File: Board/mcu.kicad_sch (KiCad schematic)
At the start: 16 parts, among them J2 Conn_01x03_Pin, U2 RP2040

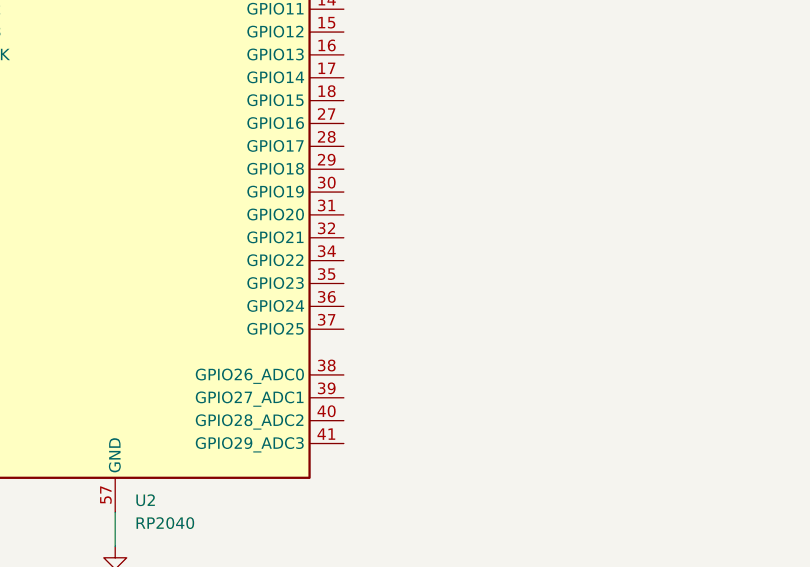
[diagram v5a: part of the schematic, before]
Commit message: Done routing all parts.
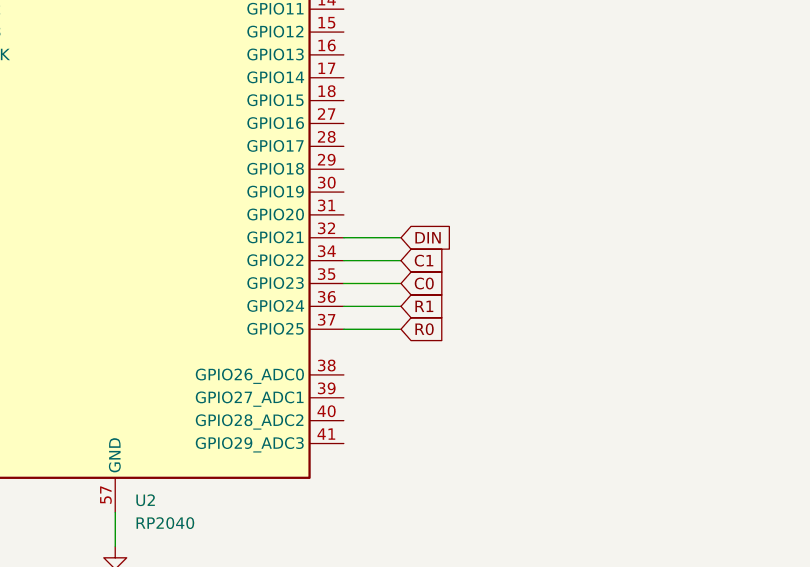
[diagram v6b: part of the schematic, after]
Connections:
- net DIN: now reaches U2.32 (GPIO21)
- net C1: now reaches U2.34 (GPIO22)
- net C0: now reaches U2.35 (GPIO23)
- net R1: now reaches U2.36 (GPIO24)
- net R0: now reaches U2.37 (GPIO25)
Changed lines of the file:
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@@
+    (stroke (width 0) (type default))
+  )
+  (wire (pts (xy 135.89 135.89) (xy 142.24 135.89))
     (stroke (width 0) (type default))
   )
@@
     (stroke (width 0) (type default))
   )
+  (wire (pts (xy 135.89 140.97) (xy 142.24 140.97))
+    (stroke (width 0) (type default))
+  )
   (wire (pts (xy 118.11 63.5) (xy 118.11 72.39))
     (stroke (width 0) (type default))
@@
     (stroke (width 0) (type default))
   )
+  (wire (pts (xy 135.89 133.35) (xy 142.24 133.35))
+    (stroke (width 0) (type default))
+  )
   (wire (pts (xy 105.41 63.5) (xy 107.95 63.5))
     (stroke (width 0) (type default))
@@
     (stroke (width 0) (type default))
   )
+  (wire (pts (xy 135.89 138.43) (xy 142.24 138.43))
+    (stroke (width 0) (type default))
+  )
   (wire (pts (xy 125.73 49.53) (xy 138.43 49.53))
     (stroke (width 0) (type default))
@@
   )
   (wire (pts (xy 115.57 63.5) (xy 113.03 63.5))
+    (stroke (width 0) (type default))
+  )
+  (wire (pts (xy 135.89 143.51) (xy 142.24 143.51))
     (stroke (width 0) (type default))
   )
@@
     )
   )
+  (global_label "R0" (shape input) (at 142.24 143.51 0) (fields_autoplaced)
+    (effects (font (size 1.27 1.27)) (justify left))
+    (property "Intersheetrefs" "${INTERSHEET_REFS}" (at 147.7047 143.51 0)
+      (effects (font (size 1.27 1.27)) (justify left) hide)
+    )
+  )
+  (global_label "R1" (shape input) (at 142.24 140.97 0) (fields_autoplaced)
+    (effects (font (size 1.27 1.27)) (justify left))
+    (property "Intersheetrefs" "${INTERSHEET_REFS}" (at 147.7047 140.97 0)
+      (effects (font (size 1.27 1.27)) (justify left) hide)
+    )
+  )
   (global_label "XOUT" (shape input) (at 82.55 135.89 180) (fields_autoplaced)
     (effects (font (size 1.27 1.27)) (justify right))
@@
     )
   )
+  (global_label "C0" (shape input) (at 142.24 138.43 0) (fields_autoplaced)
+    (effects (font (size 1.27 1.27)) (justify left))
+    (property "Intersheetrefs" "${INTERSHEET_REFS}" (at 147.7047 138.43 0)
+      (effects (font (size 1.27 1.27)) (justify left) hide)
+    )
+  )
   (global_label "XIN" (shape input) (at 82.55 125.73 180) (fields_autoplaced)
     (effects (font (size 1.27 1.27)) (justify right))
@@
     )
   )
+  (global_label "C1" (shape input) (at 142.24 135.89 0) (fields_autoplaced)
+    (effects (font (size 1.27 1.27)) (justify left))
+    (property "Intersheetrefs" "${INTERSHEET_REFS}" (at 147.7047 135.89 0)
+      (effects (font (size 1.27 1.27)) (justify left) hide)
+    )
+  )
   (global_label "QSPI_SD3" (shape input) (at 64.77 114.3 180) (fields_autoplaced)
     (effects (font (size 1.27 1.27)) (justify right))
@@
     )
   )
+  (global_label "DIN" (shape input) (at 142.24 133.35 0) (fields_autoplaced)
+    (effects (font (size 1.27 1.27)) (justify left))
+    (property "Intersheetrefs" "${INTERSHEET_REFS}" (at 148.4305 133.35 0)
+      (effects (font (size 1.27 1.27)) (justify left) hide)
+    )
+  )

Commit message: Rev 2
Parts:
- added Q1: BSS138, Package_TO_SOT_SMD:SOT-23-3, symbol dk_Transistors-FETs-MOSFETs-Single:BSS138
- added R7, R8: 10k, Resistor_SMD:R_0402_1005Metric, symbol Device:R
- added R9: 470, Resistor_SMD:R_0201_0603Metric, symbol Device:R
- J2: footprint Connector_PinHeader_2.00mm:PinHeader_1x03_P2.00mm_Vertical -> Connector_PinHeader_2.54mm:PinHeader_1x03_P2.54mm_Vertical
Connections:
- net +3.3V: now also Q1.1 (G), R7.1
- net DIN: now also Q1.3 (D), R8.2; no longer U2.32 (GPIO21)
- new net: R9.1, U2.32 (GPIO21)
- new net: Q1.2 (S), R7.2, R9.2
- new net VBUS: R8.1
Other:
- note added: "Level Shifter"

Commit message: 65% ke matrix
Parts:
- Q1: footprint Package_TO_SOT_SMD:SOT-23-3 -> digikey-footprints:SOT-23-3
- R9: footprint Resistor_SMD:R_0201_0603Metric -> Resistor_SMD:R_0603_1608Metric
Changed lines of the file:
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@@
       (effects (font (size 1.27 1.27)))
     )
-    (property "Footprint" "Resistor_SMD:R_0201_0603Metric" (at 152.4 135.128 90)
+    (property "Footprint" "Resistor_SMD:R_0603_1608Metric" (at 152.4 135.128 90)
       (effects (font (size 1.27 1.27)) hide)
     )
@@
       (effects (font (size 1.27 1.27)) hide)
     )
-    (property "Datasheet" "https://mm.digikey.com/Volume0/opasdata/d220001/medias/docus/609/CL21A106KOQNNNE_Spec.pdf" (at 38.1 146.05 0)
+    (property "Datasheet" "~" (at 38.1 146.05 0)
       (effects (font (size 1.27 1.27)) hide)
     )
@@
       (effects (font (size 1.524 1.524)))
     )
-    (property "Footprint" "Package_TO_SOT_SMD:SOT-23-3" (at 173.99 138.43 0)
+    (property "Footprint" "digikey-footprints:SOT-23-3" (at 173.99 138.43 0)
       (effects (font (size 1.524 1.524)) (justify left) hide)
     )
